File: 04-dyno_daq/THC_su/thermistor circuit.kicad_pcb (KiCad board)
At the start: 2 copper layers, 31 x 16 mm, 12 parts, among them J1 Conn_01x04, J2 Conn_01x02, U1 INA333xxDGK

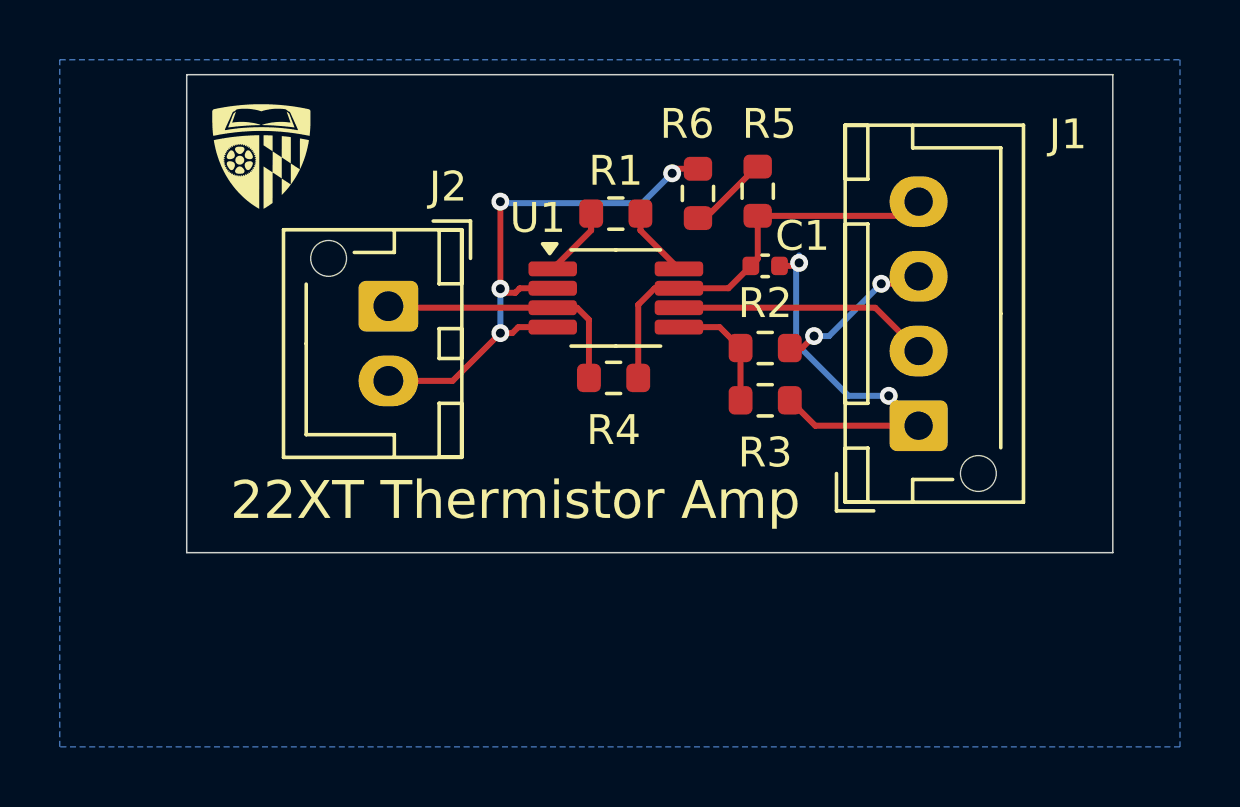
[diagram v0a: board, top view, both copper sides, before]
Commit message: Updated grounding for temp pcbs
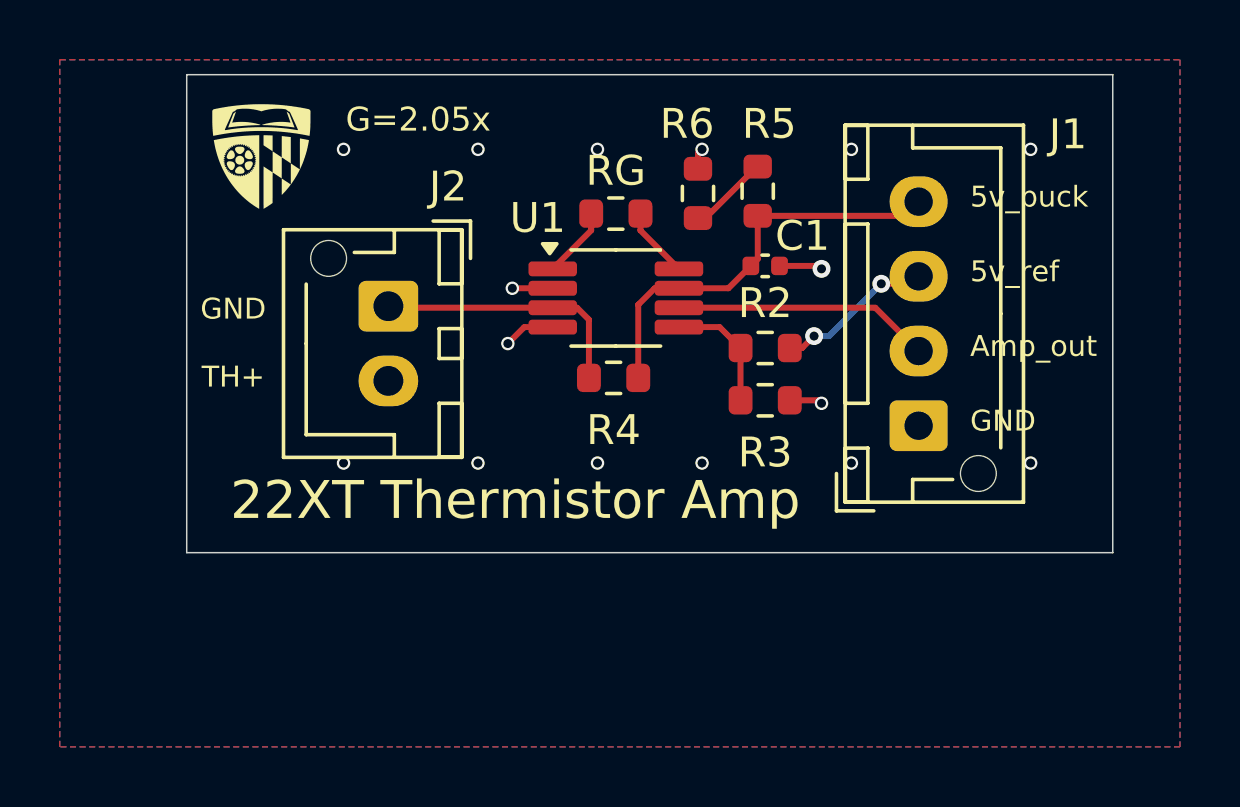
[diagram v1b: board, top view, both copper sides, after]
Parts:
- renumbered R1 to RG
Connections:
- J2 pad 1: TH+ -> GND
- J2 pad 2: GND -> TH+
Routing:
- net GND: track 33.2 -> 6.34 mm, vias 6 -> 16
- added copper zone on F.Cu, net GND
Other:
- board text added: "5v_buck"
- board text added: "5v_ref"
- board text added: "Amp_out"
- board text added: "G=2.05x"
- board text added: "GND"
- board text added: "TH+"
